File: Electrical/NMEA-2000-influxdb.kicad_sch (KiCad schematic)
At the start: 25 parts, among them J1 Conn_01x04, J2 Conn_01x04, J3 Conn_02x08, SW3 SW_Push, U1 LM7805_TO220, U2 ESP32_NODEMCU, U3 SN65HVD230, U4 SD-Card-Module, U5 SN65HVD230-Module

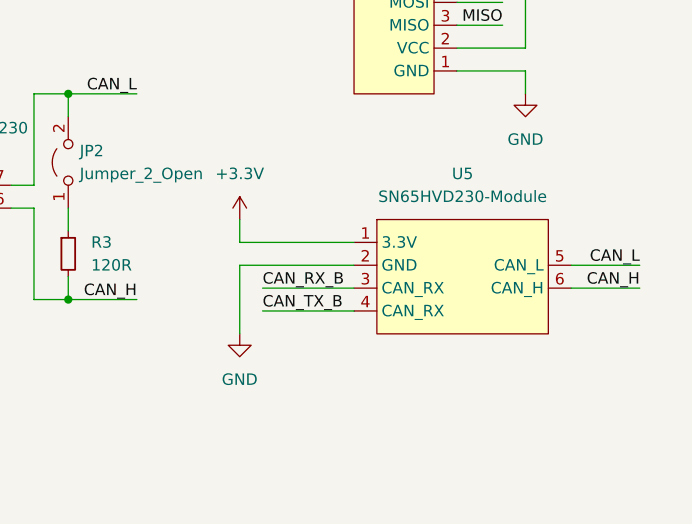
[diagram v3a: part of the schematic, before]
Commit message: Updated SN65HVD Module
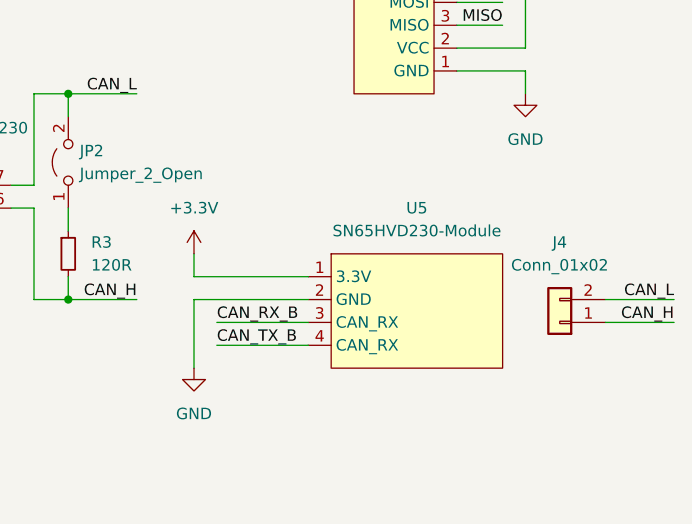
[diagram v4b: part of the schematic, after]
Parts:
- added J4: Conn_01x02, symbol Connector_Generic:Conn_01x02
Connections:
- net CAN_H: now also J4.1 (Pin_1); no longer U5.6 (CAN_H)
- net CAN_L: now also J4.2 (Pin_2); no longer U5.5 (CAN_L)
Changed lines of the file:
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@@
 	(wire
 		(pts
-			(xy 246.38 135.89) (xy 233.68 135.89)
+			(xy 241.3 139.7) (xy 228.6 139.7)
 		)
 		(stroke
@@
 	(wire
 		(pts
-			(xy 270.51 138.43) (xy 278.13 138.43)
+			(xy 274.32 142.24) (xy 281.94 142.24)
 		)
 		(stroke
@@
 	(wire
 		(pts
-			(xy 233.68 133.35) (xy 233.68 135.89)
+			(xy 228.6 137.16) (xy 228.6 139.7)
 		)
 		(stroke
@@
 	(wire
 		(pts
-			(xy 233.68 138.43) (xy 233.68 146.05)
+			(xy 228.6 142.24) (xy 228.6 149.86)
 		)
 		(stroke
@@
 	(wire
 		(pts
-			(xy 236.22 140.97) (xy 246.38 140.97)
+			(xy 231.14 144.78) (xy 241.3 144.78)
 		)
 		(stroke
@@
 	(wire
 		(pts
-			(xy 270.51 140.97) (xy 278.13 140.97)
+			(xy 274.32 144.78) (xy 281.94 144.78)
 		)
 		(stroke
@@
 	(wire
 		(pts
-			(xy 236.22 143.51) (xy 246.38 143.51)
+			(xy 231.14 147.32) (xy 241.3 147.32)
 		)
 		(stroke
@@
 	(wire
 		(pts
-			(xy 246.38 138.43) (xy 233.68 138.43)
+			(xy 241.3 142.24) (xy 228.6 142.24)
 		)
 		(stroke
@@
 	)
 	(label "CAN_RX_B"
-		(at 236.22 140.97 0)
+		(at 231.14 144.78 0)
 		(fields_autoplaced yes)
 		(effects
@@
 	)
 	(label "CAN_L"
-		(at 278.13 138.43 180)
+		(at 281.94 142.24 180)
 		(fields_autoplaced yes)
 		(effects
@@
 	)
 	(label "CAN_H"
-		(at 278.13 140.97 180)
+		(at 281.94 144.78 180)
 		(fields_autoplaced yes)
 		(effects
@@
 	)
 	(label "CAN_TX_B"
-		(at 236.22 143.51 0)
+		(at 231.14 147.32 0)
 		(fields_autoplaced yes)
 		(effects
@@
 	)
 	(symbol
+		(lib_id "Connector_Generic:Conn_01x02")
+		(at 269.24 144.78 180)
+		(unit 1)
+		(exclude_from_sim no)
+		(in_bom yes)
+		(on_board yes)
+		(dnp no)
+		(fields_autoplaced yes)
+		(property "Reference" "J4"
+			(at 269.24 135.89 0)
+			(effects
+				(font
+					(size 1.27 1.27)
+				)
+			)
+		)
+		(property "Value" "Conn_01x02"
+			(at 269.24 138.43 0)
+			(effects
+				(font
+					(size 1.27 1.27)
+				)
+			)
+		)
+		(property "Footprint" ""
+			(at 269.24 144.78 0)
+			(effects
+				(font
+					(size 1.27 1.27)
+				)
+				(hide yes)
+			)
+		)
+		(property "Datasheet" "~"
+			(at 269.24 144.78 0)
+			(effects
+				(font
+					(size 1.27 1.27)
+				)
+				(hide yes)
+			)
+		)
+		(property "Description" "Generic connector, single row, 01x02, script generated (kicad-library-utils/schlib/autogen/connector/)"
+			(at 269.24 144.78 0)
+			(effects
+				(font
+					(size 1.27 1.27)
+				)
+				(hide yes)
+			)
+		)
+		(pin "1"
+		)
+		(pin "2"
+		)
+		(instances
+			(project "NMEA-2000-influxdb"
+				(path "/efe7a42c-525a-4afc-8476-4cc785240ca6"
+					(reference "J4")
+					(unit 1)
+				)
+			)
+		)
+	)
+	(symbol
 		(lib_id "Device:R")
 		(at 232.41 60.96 0)
@@
 	(symbol
 		(lib_id "sn65hvd230-module:SN65HVD230-Module")
-		(at 257.81 133.35 0)
+		(at 252.73 137.16 0)
 		(unit 1)
 		(exclude_from_sim no)
@@
 		(fields_autoplaced yes)
 		(property "Reference" "U5"
-			(at 258.445 128.27 0)
+			(at 253.365 132.08 0)
 			(effects
 				(font
@@
 		)
 		(property "Value" "SN65HVD230-Module"
-			(at 258.445 130.81 0)
+			(at 253.365 134.62 0)
 			(effects
 				(font
@@
 		)
 		(property "Footprint" "Connector_PinSocket_2.54mm:PinSocket_1x04_P2.54mm_Horizontal"
-			(at 256.54 133.35 0)
+			(at 251.46 137.16 0)
 			(effects
 				(font
@@
 		)
 		(property "Datasheet" ""
-			(at 256.54 133.35 0)
+			(at 251.46 137.16 0)
 			(effects
 				(font
@@
 		)
 		(property "Description" ""
-			(at 257.81 133.35 0)
+			(at 252.73 137.16 0)
 			(effects
 				(font
@@
 			)
 		)
-		(pin "6"
-		)
 		(pin "4"
 		)
@@
 		(pin "2"
 		)
-		(pin "5"
-		)
 		(instances
 			(project "NMEA-2000-influxdb"
@@
 	(symbol
 		(lib_id "power:+3.3V")
-		(at 233.68 133.35 0)
+		(at 228.6 137.16 0)
 		(unit 1)
 		(exclude_from_sim no)
@@
 		(fields_autoplaced yes)
 		(property "Reference" "#PWR018"
-			(at 233.68 137.16 0)
+			(at 228.6 140.97 0)
 			(effects
 				(font
@@
 		)
 		(property "Value" "+3.3V"
-			(at 233.68 128.27 0)
+			(at 228.6 132.08 0)
 			(effects
 				(font
@@
 		)
 		(property "Footprint" ""
-			(at 233.68 133.35 0)
+			(at 228.6 137.16 0)
 			(effects
 				(font
@@
 		)
 		(property "Datasheet" ""
-			(at 233.68 133.35 0)
+			(at 228.6 137.16 0)
 			(effects
 				(font
@@
 		)
 		(property "Description" "Power symbol creates a global label with name \"+3.3V\""
-			(at 233.68 133.35 0)
+			(at 228.6 137.16 0)
 			(effects
 				(font
@@
 		(lib_name "GND_3")
 		(lib_id "power:GND")
-		(at 233.68 146.05 0)
+		(at 228.6 149.86 0)
 		(unit 1)
 		(exclude_from_sim no)
@@
 		(fields_autoplaced yes)
 		(property "Reference" "#PWR019"
-			(at 233.68 152.4 0)
+			(at 228.6 156.21 0)
 			(effects
 				(font
@@
 		)
 		(property "Value" "GND"
-			(at 233.68 151.13 0)
+			(at 228.6 154.94 0)
 			(effects
 				(font
@@
 		)
 		(property "Footprint" ""
-			(at 233.68 146.05 0)
+			(at 228.6 149.86 0)
 			(effects
 				(font
@@
 		)
 		(property "Datasheet" ""
-			(at 233.68 146.05 0)
+			(at 228.6 149.86 0)
 			(effects
 				(font
@@
 		)
 		(property "Description" "Power symbol creates a global label with name \"GND\" , ground"
-			(at 233.68 146.05 0)
+			(at 228.6 149.86 0)
 			(effects
 				(font

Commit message: Cleared up project
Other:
- removed sheet Display
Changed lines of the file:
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@@
 		(on_board yes)
 		(dnp no)
-		(fields_autoplaced yes)
 		(property "Reference" "#PWR038"
 			(at 53.34 127 0)
@@
 		)
 		(property "Value" "GND"
-			(at 53.34 125.73 0)
+			(at 53.086 124.714 0)
 			(effects
 				(font
@@
 		(on_board yes)
 		(dnp no)
-		(fields_autoplaced yes)
 		(property "Reference" "#PWR039"
 			(at 83.82 111.76 0)
@@
 		)
 		(property "Value" "+12V"
-			(at 83.82 102.87 0)
+			(at 83.82 103.378 0)
 			(effects
 				(font
@@
 		(on_board yes)
 		(dnp no)
-		(fields_autoplaced yes)
 		(property "Reference" "#PWR040"
 			(at 83.82 127 0)
@@
 		)
 		(property "Value" "GND"
-			(at 83.82 125.73 0)
+			(at 83.82 124.714 0)
 			(effects
 				(font
@@
 				)
 			)
-		)
-	)
-	(sheet
-		(at 26.924 138.938)
-		(size 49.53 16.51)
-		(fields_autoplaced yes)
-		(stroke
-			(width 0.1524)
-			(type solid)
-		)
-		(fill
-			(color 0 0 0 0.0000)
-		)
-		(property "Sheetname" "Display"
-			(at 26.924 138.2264 0)
-			(effects
-				(font
-					(size 1.27 1.27)
-				)
-				(justify left bottom)
-			)
-		)
-		(property "Sheetfile" "display.kicad_sch"
-			(at 26.924 156.0326 0)
-			(effects
-				(font
-					(size 1.27 1.27)
-				)
-				(justify left top)
-			)
-		)
-		(instances
-			(project "NMEA-2000-influxdb"
-				(path "/efe7a42c-525a-4afc-8476-4cc785240ca6"
-					(page "2")
-				)
-			)

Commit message: Updated Schematic
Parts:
- removed C3: 0.1uF, symbol Device:C
- removed HS1: Heatsink, symbol Mechanical:Heatsink
- removed R26: 330R, symbol Device:R
- removed SW3: SW_Push, symbol Switch:SW_Push
- added R4: 330R, Resistor_THT:R_Axial_DIN0204_L3.6mm_D1.6mm_P5.08mm_Horizontal, symbol Device:R
- A1: footprint MPCNC_Shield_Footprints:LM2596_Step_Down_Module-21.3x43.6mm -> LM2596:LM2596_Step_Down_Module-21.3x43.6mm
- D1: renamed from D7; footprint (none) -> LED_THT:LED_D3.0mm
- D2: renamed from D8; footprint (none) -> LED_THT:LED_D3.0mm
- D3: renamed from D9; footprint (none) -> LED_THT:LED_D3.0mm
- D4: renamed from D10; footprint (none) -> LED_THT:LED_D3.0mm
- J3: renamed from J4; footprint (none) -> Connector_PinSocket_2.54mm:PinSocket_1x02_P2.54mm_Vertical
- R1: renamed from R2; footprint (none) -> Resistor_THT:R_Axial_DIN0204_L3.6mm_D1.6mm_P5.08mm_Horizontal
- R2: renamed from R10; footprint (none) -> Resistor_THT:R_Axial_DIN0204_L3.6mm_D1.6mm_P5.08mm_Horizontal
- R3: renamed from R25; footprint (none) -> Resistor_THT:R_Axial_DIN0204_L3.6mm_D1.6mm_P5.08mm_Horizontal
- renumbered J3 to J4, JP2 to JP1, JP1 to JP2, R3 to R5, U4 to U3, U3 to U4
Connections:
- net +3.3V: now also R4.1
- net at D4.2 (A): now also R4.2
- no-connect marks 12 -> 13

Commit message: Cleared up Schematic
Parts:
- added C3, C4: 0.1uF, Capacitor_THT:C_Disc_D9.0mm_W5.0mm_P7.50mm, symbol Device:C_Small
- added H1, H2, H3, H4: MountingHole_Pad, MountingHole:MountingHole_3mm_Pad_Via, symbol Mechanical:MountingHole_Pad
- C1: value 0.33uF -> 0.1uF
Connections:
- net +12V: now also C3.1, C4.1
- net GND: now also C3.2, C4.2, H1.1, H2.1, H3.1, H4.1
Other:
- moved on the sheet: A1, C1, C2, D1, D2, D3, D4, J3, J4, JP1, JP2, R1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

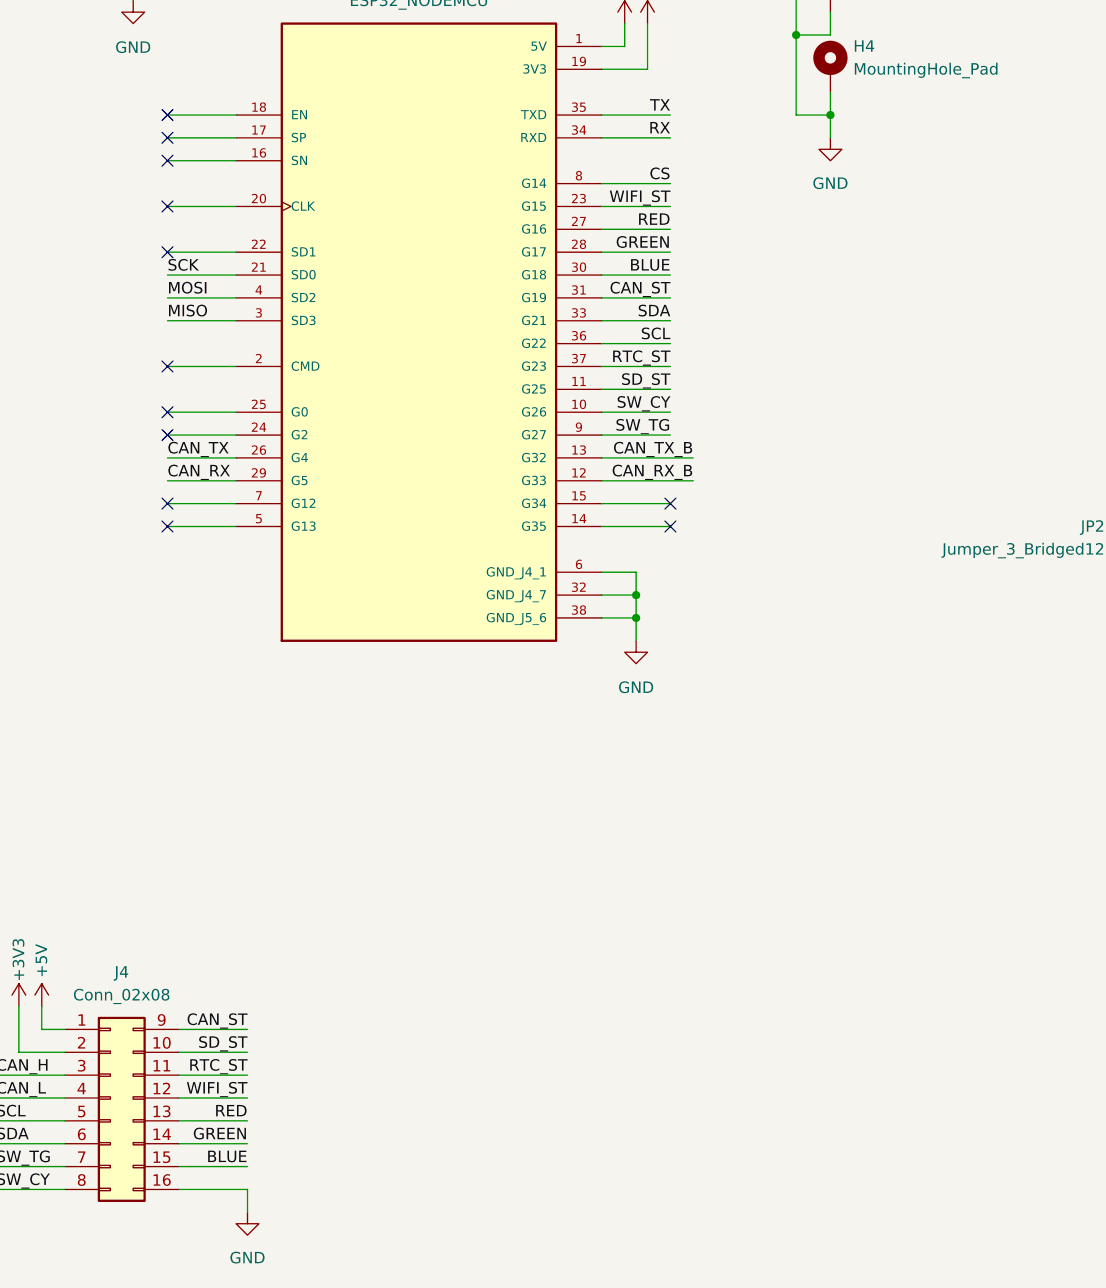
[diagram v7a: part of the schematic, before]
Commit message: Added SMD SD-Card
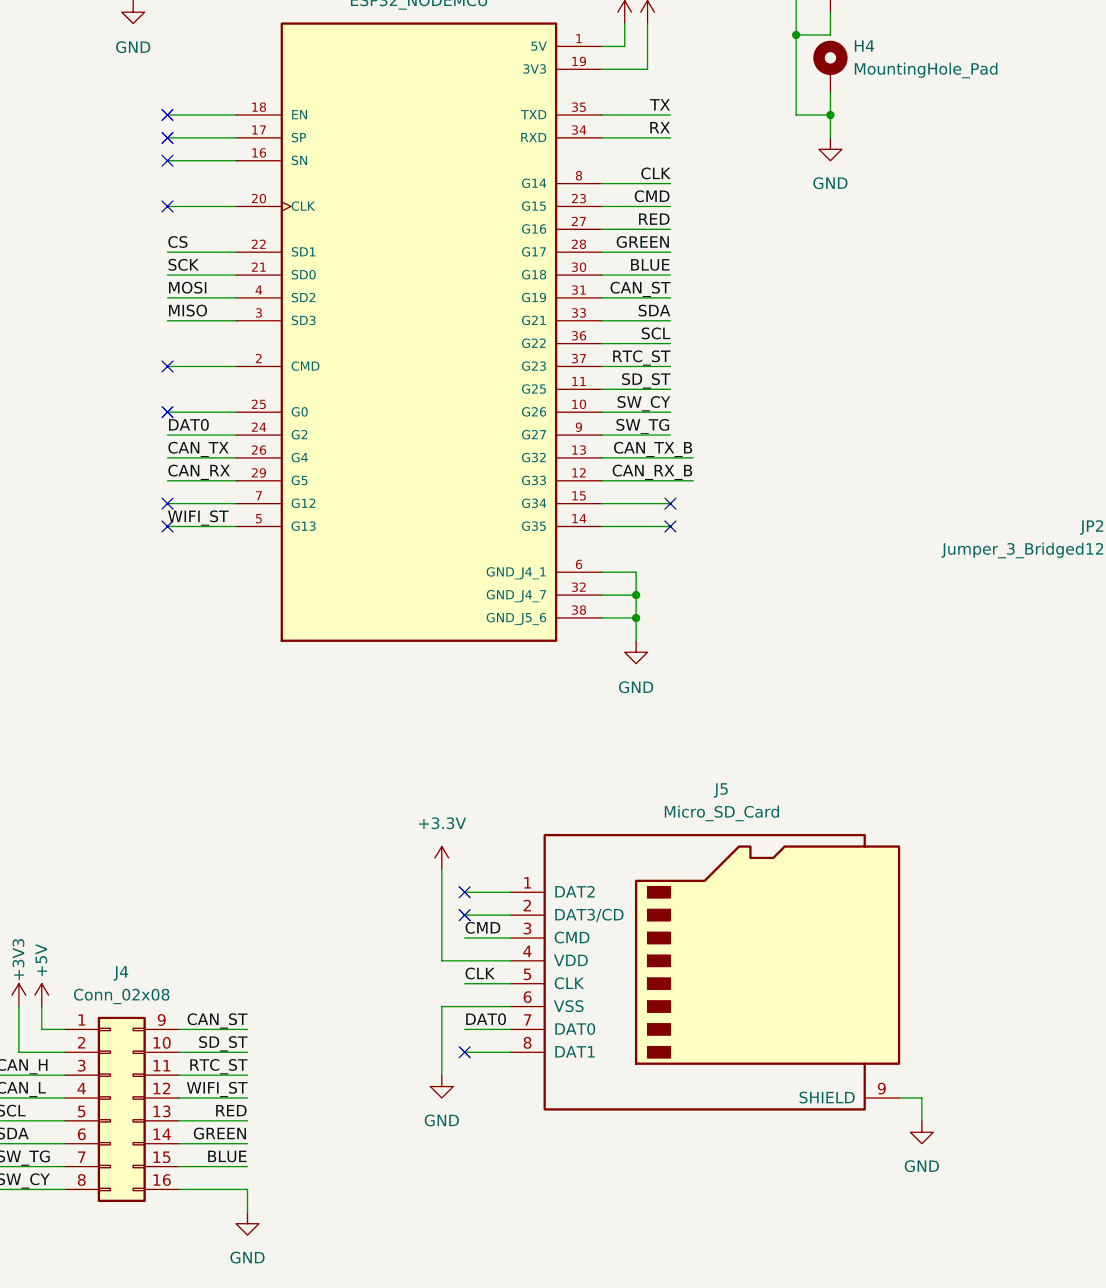
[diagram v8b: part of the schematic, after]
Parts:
- added J5: Micro_SD_Card, Connector_Card:microSD_HC_Hirose_DM3AT-SF-PEJM5, symbol Connector:Micro_SD_Card
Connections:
- net +3.3V: now also J5.4 (VDD)
- net CS: now also U2.22 (SD1); no longer U2.8 (G14)
- net GND: now also J5.6 (VSS), J5.9 (SHIELD)
- net WIFI_ST: now also U2.5 (G13); no longer U2.23 (G15)
- net DAT0: now reaches U2.24 (G2)
- net DAT0: now also J5.7 (DAT0)
- new net CLK: J5.5 (CLK), U2.8 (G14)
- new net CMD: J5.3 (CMD), U2.23 (G15)
- no-connect marks 13 -> 14
